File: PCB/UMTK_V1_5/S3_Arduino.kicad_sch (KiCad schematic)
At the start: 0 parts

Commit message: Put in Files for V1
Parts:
- added C10, C5, C6, C7, C8, C9: 0.1u, Ceramic Cap 5mm, symbol UMTK-altium-import:root_0_Cap
- added J1: NakedMega, Arduino Mega, symbol UMTK-altium-import:root_3_NakedMega
- added R33, R34, R35, R36, R37, R38, R39, R40, R41, R42, R43, R46, R48, R49, R50, R51: Res1, AXIAL-0.3-3D, symbol UMTK-altium-import:root_3_Res1
- added R44, R45, R47, R52, R53, R54, R55: Res1, AXIAL-0.3-3D, symbol UMTK-altium-import:root_0_Res1
- added SW1, SW2, SW3, SW4, SW5, SW6: Tac Switch, TacSwitch, symbol UMTK-altium-import:root_0_Tac Switch
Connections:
- new net: C8.1, R49.2, R53.1, SW4.2
- new net: R39.2, R40.1
- new net: R40.2, R41.1
- new net: C10.1, R51.2, R55.1, SW6.2
- new net: R33.2, R34.1
- new net: R34.2, R35.1
- new net: C9.1, R50.2, R54.1, SW5.2
- new net: C5.1, R43.2, R44.1, SW1.2
- new net: J1.D4, R37.1
- new net: C7.1, R48.2, R52.1, SW3.2
- new net: C6.1, R46.2, R47.1, SW2.2
- new net: J1.D3, R45.2
- new net +5: J1.EXT5V, R43.1, R46.1, R48.1, R49.1, R50.1, R51.1
- new net D1_A: J1.D33
- new net D1_B: J1.D35
- new net D1_C: J1.D29
- new net D1_D: J1.D31
- new net D1_D1: J1.D24
- new net D1_D2: J1.D25
- new net D1_D3: J1.D26
- new net D1_D4: J1.D27
- new net D1_DP: J1.D30
- new net D1_E: J1.D32
- new net D1_F: J1.D34
- new net D1_G: J1.D28
- new net D1_OE: J1.D36
- new net D2_A: J1.D42
- new net D2_B: J1.D44
- new net D2_C: J1.D38
- new net D2_D: J1.D40
- new net D2_DP: J1.D39
- new net D2_E: J1.D41
- new net D2_F: J1.D43
- new net D2_G: J1.D37
- new net D2_OE: J1.D45
- new net GND: C10.2, C5.2, C6.2, C7.2, C8.2, C9.2, J1.GND, R36.2, R38.2, R42.2, SW1.3, SW2.3, SW3.3, SW4.3, SW5.3, SW6.3
- new net LC_DT: J1.D6
- new net LC_SCK: J1.D5
- new net M_DISABLE: J1.D7
- new net M_EN/IN1: J1.D8
- new net M_FAULT: J1.D12
- new net M_ISENS: J1.A2
- new net M_ITRIP: J1.D10
- new net M_OL: J1.D11
- new net M_PH/IN2: J1.D9
- new net SLIDE_CLK: R37.2, R38.1
- new net SLIDE_DAT: R45.1
- new net SW_1: J1.A5, R52.2
- new net SW_2: J1.A6, R53.2
- new net SW_3: J1.A7, R54.2
- new net SW_4: J1.A8, R55.2
- new net SW_5: J1.A9, R44.2
- new net SW_6: J1.A10, R47.2
- new net Vin: R33.1
- new net Vin_sens: J1.A0, R35.2, R36.1
- new net Vmot: R39.1
- new net Vmot_sens: J1.A1, R41.2, R42.1
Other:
- note added: "Arduino"
- note added: "Buttons 1-4"
- note added: "Buttons 5-6"

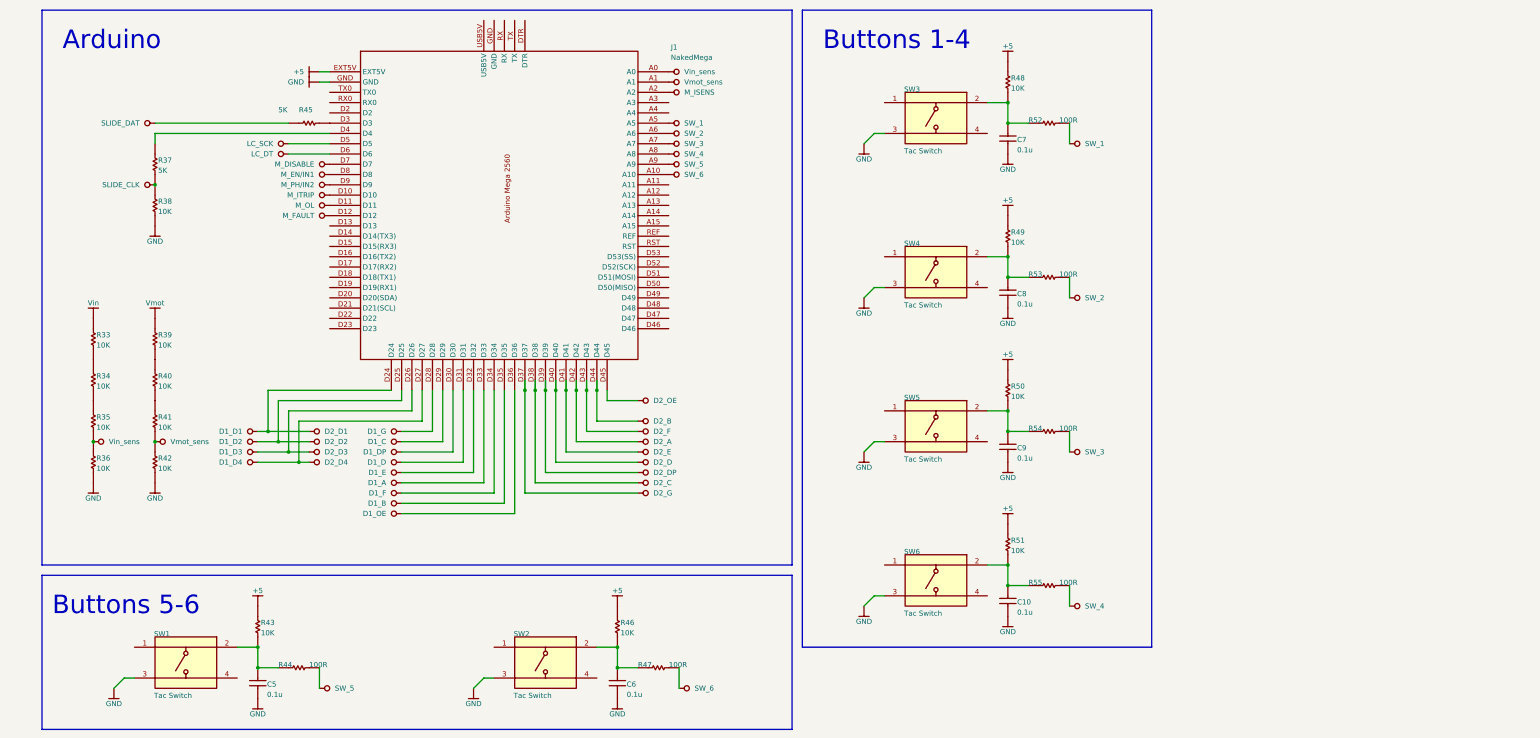
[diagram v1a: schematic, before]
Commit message: Updated Schematics
Done: 7 Seg, Power, Motor, Slide, HX711
To Do: Arduino
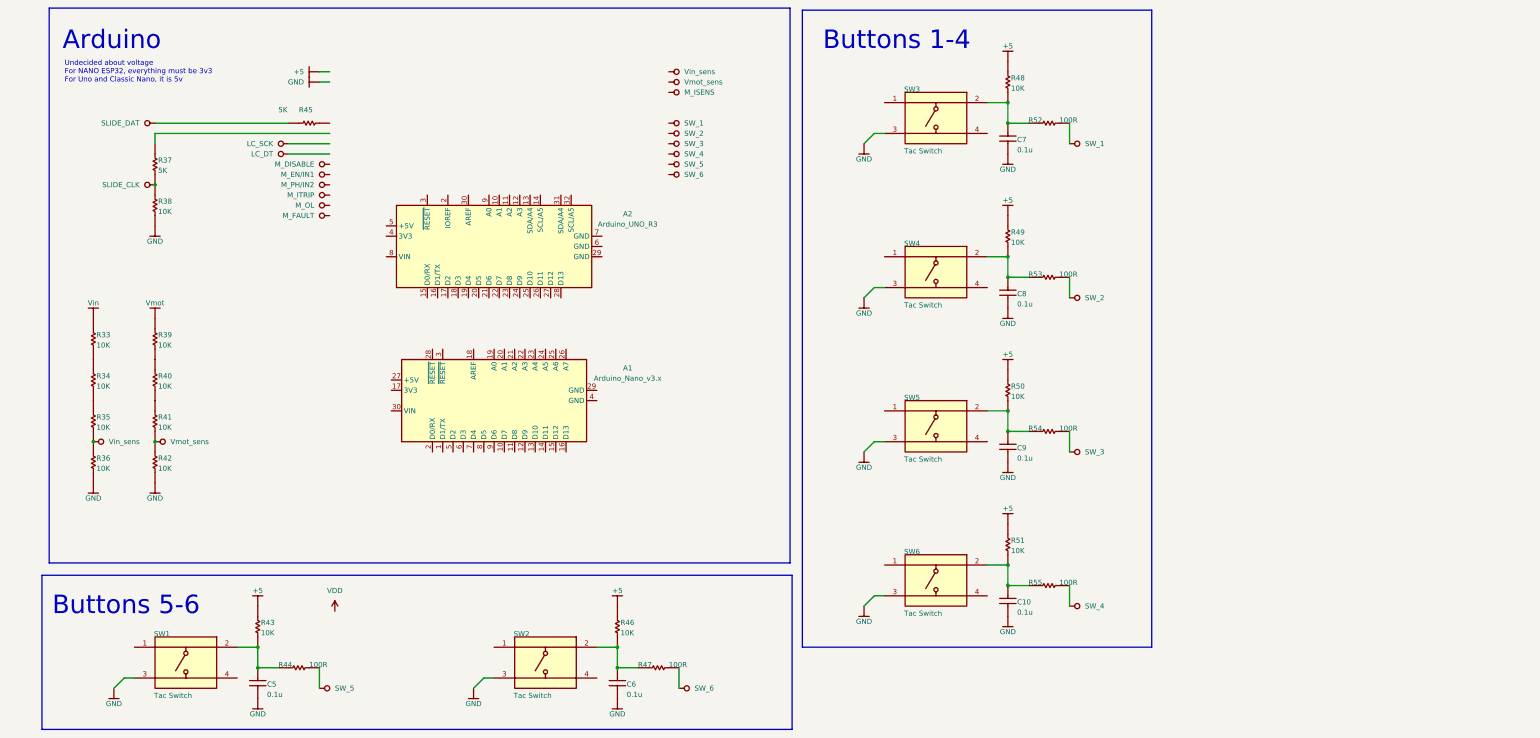
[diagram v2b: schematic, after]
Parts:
- removed J1: NakedMega, Arduino Mega, symbol UMTK-altium-import:root_3_NakedMega
- added A1: Arduino_Nano_v3.x, Module:Arduino_Nano, symbol MCU_Module:Arduino_Nano_v3.x
- added A2: Arduino_UNO_R3, Module:Arduino_UNO_R3, symbol MCU_Module:Arduino_UNO_R3
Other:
- note added: "Undecided about voltage For NANO ESP32, everything must be 3v3 For Uno and Classic Nano, it is 5v"

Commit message: Updating Schematic
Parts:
- removed A1: Arduino_Nano_v3.x, Module:Arduino_Nano, symbol MCU_Module:Arduino_Nano_v3.x
- removed A2: Arduino_UNO_R3, Module:Arduino_UNO_R3, symbol MCU_Module:Arduino_UNO_R3
- removed C10, C5, C6, C7, C8, C9: 0.1u, Ceramic Cap 5mm, symbol UMTK-altium-import:root_0_Cap
- removed R33, R34, R35, R36, R39, R40, R41, R42, R43, R46, R48, R49, R50, R51: Res1, AXIAL-0.3-3D, symbol UMTK-altium-import:root_3_Res1
- removed R44, R47, R52, R53, R54, R55: Res1, AXIAL-0.3-3D, symbol UMTK-altium-import:root_0_Res1
- removed SW1, SW2, SW3, SW4, SW5, SW6: Tac Switch, TacSwitch, symbol UMTK-altium-import:root_0_Tac Switch
- added A1: Arduino_Mega2560_R3_Shield, PCM_arduino-library:Arduino_Mega2560_R3_Shield, symbol arduino-library:Arduino_Mega2560_R3_Shield
- added C1, C2, C3, C4, C5, C6: 0.1u, symbol Device:C
- added R10, R12, R14, R15, R16, R17, R18, R19, R2, R20, R21, R4, R6, R8: 10k, symbol Device:R_US
- added R11, R13, R3, R5, R7, R9: 100r, symbol Device:R_US
- added S1, S2, S3, S4, S5, S6: FSM4JSMATR, digikey-footprints:Switch_Tactile_SMD_6x6mm, symbol dk_Tactile-Switches:FSM4JSMATR
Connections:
- net GND: now also C1.1, C2.1, C3.1, C4.1, C5.1, C6.1, R17.2, R21.2, S1.2, S2.2, S3.2, S4.2, S5.2, S6.2
- net SW_1: now also R5.2
- net SW_2: now also R7.2
- net SW_3: now also R9.2
- net SW_4: now also R11.2
- net SW_6: now also R13.2, R3.2
- net VDD: now also R10.2, R12.2, R2.2, R4.2, R6.2, R8.2
- new net: C1.2, R2.1, R3.1, S1.3
- new net: C4.2, R8.1, R9.1, S4.3
- new net: C5.2, R10.1, R11.1, S5.3
- new net: C6.2, R12.1, R13.1, S6.3
- new net: C3.2, R6.1, R7.1, S3.3
- new net: C2.2, R4.1, R5.1, S2.3
- new net: R14.2, R15.1
- new net: R15.2, R16.1
- new net: R18.2, R19.1
- new net: R19.2, R20.1
- new net +12V: R14.1
- new net VMOTOR: R18.1
- new net VM_Sense: R20.2, R21.1
- new net Vin_Sense: R16.2, R17.1
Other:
- note added: "Buttons"
- note removed: "Buttons 1-4"
- note removed: "Buttons 5-6"
- moved on the sheet: R37, R38, R45

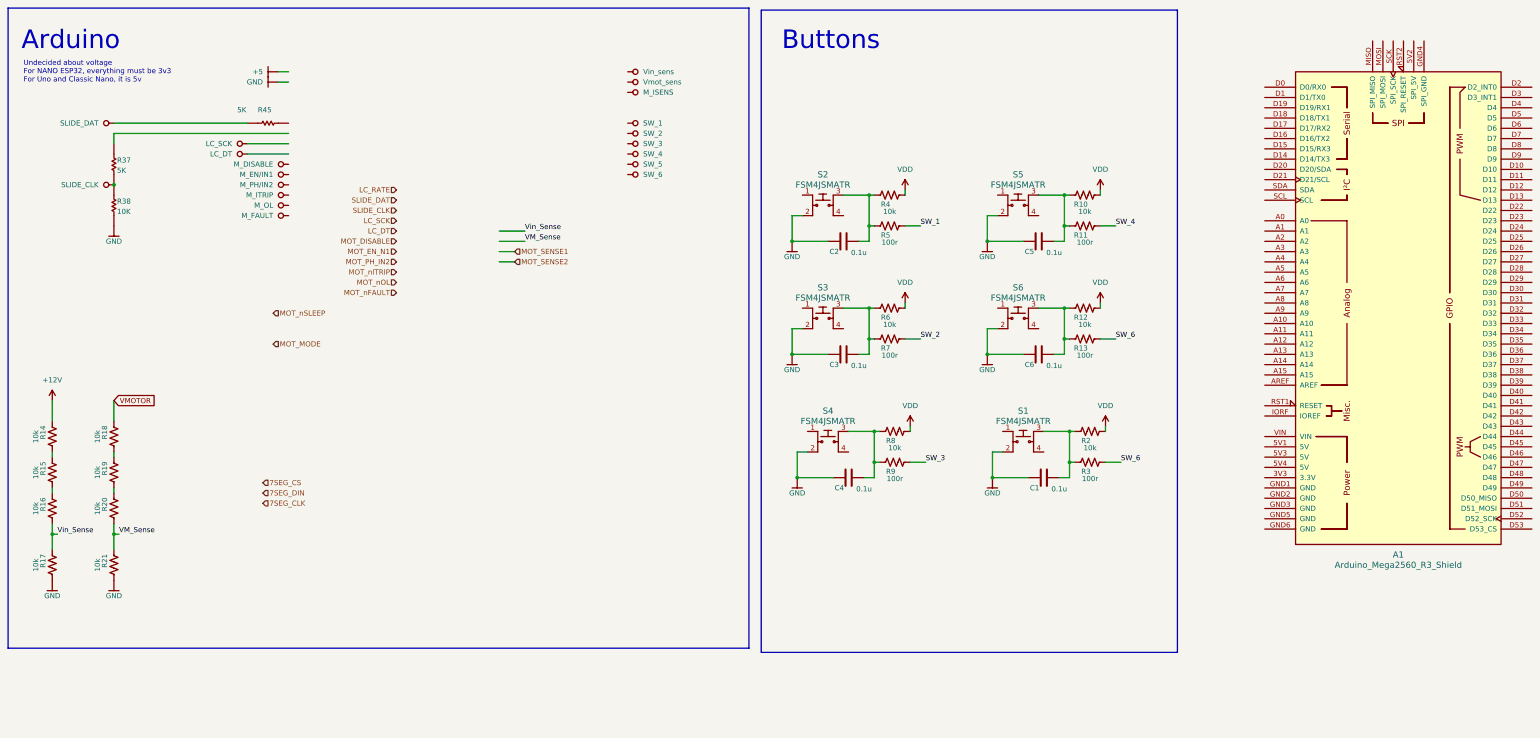
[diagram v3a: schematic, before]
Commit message: Schematic Done, Assigning footprint
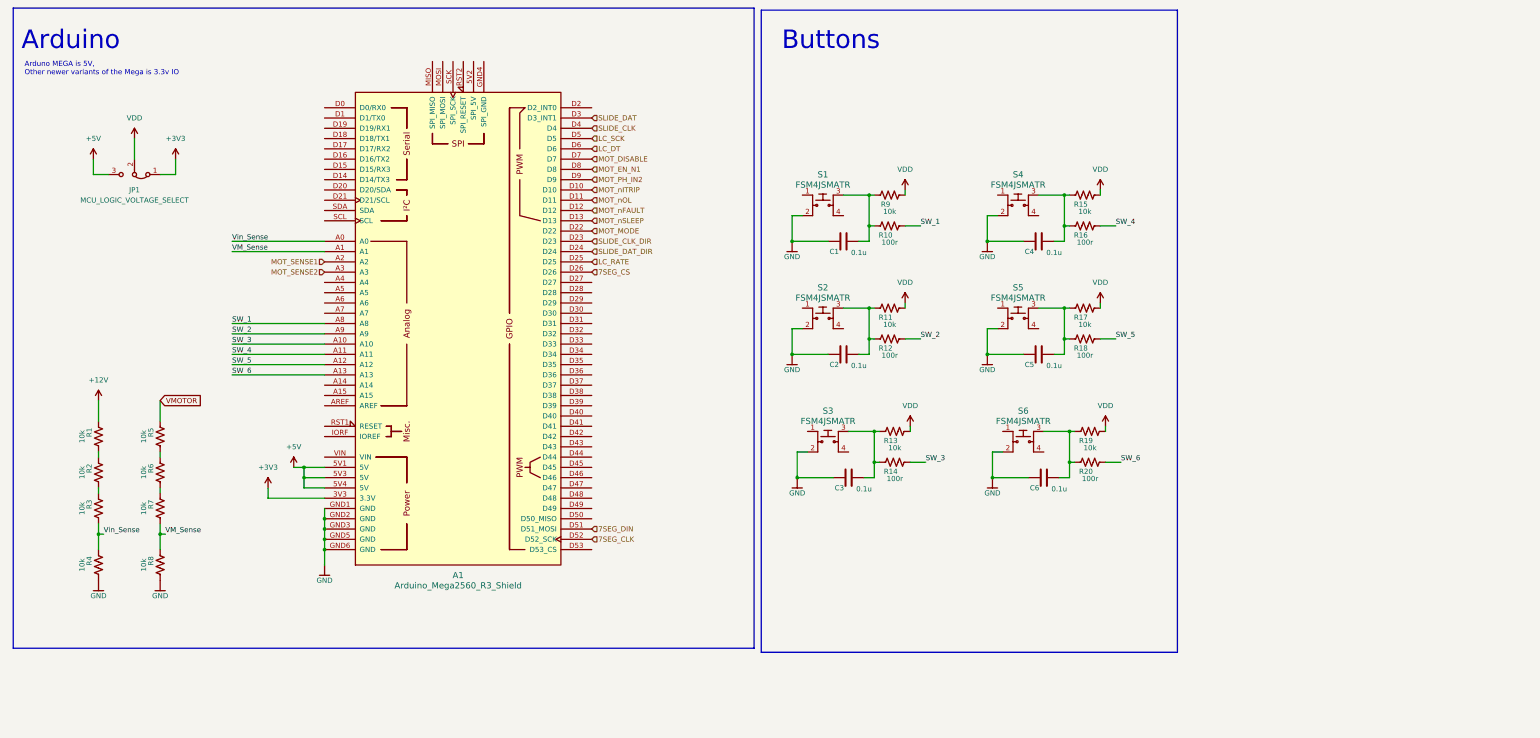
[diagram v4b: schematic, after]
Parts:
- removed R37, R38: Res1, AXIAL-0.3-3D, symbol UMTK-altium-import:root_3_Res1
- removed R45: Res1, AXIAL-0.3-3D, symbol UMTK-altium-import:root_0_Res1
- added JP1: MCU_LOGIC_VOLTAGE_SELECT, symbol Jumper:Jumper_3_Bridged12
- renumbered C2 to C1, C3 to C2, C4 to C3, C5 to C4, C6 to C5, C1 to C6, R14 to R1, R5 to R10, R6 to R11, R7 to R12, R8 to R13, R9 to R14, R10 to R15, R11 to R16, R12 to R17, R13 to R18, R2 to R19, R15 to R2, R3 to R20, R16 to R3, R17 to R4, R18 to R5, R19 to R6, R20 to R7, R21 to R8, R4 to R9, S2 to S1, S3 to S2, S4 to S3, S5 to S4, S6 to S5, S1 to S6
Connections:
- net 7SEG_CLK: now also A1.D52 (D52_SCK)
- net 7SEG_CS: now also A1.D26
- net 7SEG_DIN: now also A1.D51 (D51_MOSI)
- net GND: now also A1.GND1 (GND), A1.GND2 (GND), A1.GND3 (GND), A1.GND5 (GND), A1.GND6 (GND)
- net LC_DT: now also A1.D6
- net LC_RATE: now also A1.D25
- net LC_SCK: now also A1.D5
- net MOT_DISABLE: now also A1.D7
- net MOT_EN_N1: now also A1.D8
- net MOT_MODE: now also A1.D22
- net MOT_PH_IN2: now also A1.D9
- net MOT_SENSE1: now also A1.A2
- net MOT_SENSE2: now also A1.A3
- net MOT_nFAULT: now also A1.D12
- net MOT_nITRIP: now also A1.D10
- net MOT_nOL: now also A1.D11
- net MOT_nSLEEP: now also A1.D13
- net SLIDE_CLK: now also A1.D4
- net SLIDE_DAT: now also A1.D3 (D3_INT1)
- net SW_1: now also A1.A8
- net SW_2: now also A1.A9
- net SW_3: now also A1.A10
- net SW_4: now also A1.A11
- net SW_5: now also A1.A12, R18.2
- net SW_6: now also A1.A13; no longer R18.2
- net VDD: now also JP1.2 (C)
- net VM_Sense: now also A1.A1
- net Vin_Sense: now also A1.A0
- net +3V3: now reaches A1.3V3 (3.3V)
- net +3V3: now also JP1.1 (A)
- net +5V: now reaches A1.5V1 (5V)
- net +5V: now also A1.5V3 (5V), A1.5V4 (5V), JP1.3 (B)
- net SLIDE_CLK_DIR: now reaches A1.D23
- net SLIDE_DAT_DIR: now reaches A1.D24
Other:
- note added: "Arduno MEGA is 5V, Other newer variants of the Mega is 3.3v IO"
- note removed: "Undecided about voltage For NANO ESP32, everything must be 3v3 For Uno and Classic Nano, it is 5v"
- moved on the sheet: A1, R1, R2, R3, R4, R5, R6, R7, R8

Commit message: Footprint assign
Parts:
- A1: footprint PCM_arduino-library:Arduino_Mega2560_R3_Shield -> arduino-library:Arduino_Mega2560_R3_Shield
- C1, C2, C3, C4, C5, C6: footprint (none) -> Capacitor_SMD:C_0402_1005Metric
- JP1: footprint (none) -> Jumper:SolderJumper-3_P1.3mm_Bridged12_Pad1.0x1.5mm
- R1, R10, R11, R12, R13, R14, R15, R16, R17, R18, R19, R2, R20, R3, R4, R5, R6, R7, R8, R9: footprint (none) -> Resistor_SMD:R_0402_1005Metric
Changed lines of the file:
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@@
 			)
 		)
-		(property "Footprint" ""
+		(property "Footprint" "Resistor_SMD:R_0402_1005Metric"
 			(at 222.504 131.064 90)
 			(effects
@@
 			)
 		)
-		(property "Footprint" ""
+		(property "Footprint" "Capacitor_SMD:C_0402_1005Metric"
 			(at 261.62 76.5048 0)
 			(effects
@@
 			)
 		)
-		(property "Footprint" ""
+		(property "Footprint" "Resistor_SMD:R_0402_1005Metric"
 			(at 269.494 65.024 90)
 			(effects
@@
 			)
 		)
-		(property "Footprint" ""
+		(property "Footprint" "Resistor_SMD:R_0402_1005Metric"
 			(at 26.416 157.734 90)
 			(effects
@@
 			)
 		)
-		(property "Footprint" ""
+		(property "Footprint" "Resistor_SMD:R_0402_1005Metric"
 			(at 269.494 92.964 90)
 			(effects
@@
 			)
 		)
-		(property "Footprint" ""
+		(property "Footprint" "Capacitor_SMD:C_0402_1005Metric"
 			(at 261.62 104.4448 0)
 			(effects
@@
 			)
 		)
-		(property "Footprint" ""
+		(property "Footprint" "Capacitor_SMD:C_0402_1005Metric"
 			(at 213.36 76.5048 0)
 			(effects
@@
 			)
 		)
-		(property "Footprint" ""
+		(property "Footprint" "Resistor_SMD:R_0402_1005Metric"
 			(at 270.764 131.064 90)
 			(effects
@@
 			)
 		)
-		(property "Footprint" ""
+		(property "Footprint" "Resistor_SMD:R_0402_1005Metric"
 			(at 26.416 134.874 90)
 			(effects
@@
 			)
 		)
-		(property "Footprint" ""
+		(property "Footprint" "Jumper:SolderJumper-3_P1.3mm_Bridged12_Pad1.0x1.5mm"
 			(at 34.29 60.96 0)
 			(effects
@@
 			)
 		)
-		(property "Footprint" ""
+		(property "Footprint" "Resistor_SMD:R_0402_1005Metric"
 			(at 221.234 92.964 90)
 			(effects
@@
 			)
 		)
-		(property "Footprint" ""
+		(property "Footprint" "Resistor_SMD:R_0402_1005Metric"
 			(at 270.764 123.444 90)
 			(effects
@@
 			)
 		)
-		(property "Footprint" ""
+		(property "Footprint" "Resistor_SMD:R_0402_1005Metric"
 			(at 41.656 157.734 90)
 			(effects
@@
 			)
 		)
-		(property "Footprint" ""
+		(property "Footprint" "Resistor_SMD:R_0402_1005Metric"
 			(at 269.494 100.584 90)
 			(effects
@@
 			)
 		)
-		(property "Footprint" ""
+		(property "Footprint" "Resistor_SMD:R_0402_1005Metric"
 			(at 41.656 125.984 90)
 			(effects
@@
 			)
 		)
-		(property "Footprint" ""
+		(property "Footprint" "Resistor_SMD:R_0402_1005Metric"
 			(at 221.234 100.584 90)
 			(effects
@@
 			)
 		)
-		(property "Footprint" ""
+		(property "Footprint" "Capacitor_SMD:C_0402_1005Metric"
 			(at 213.36 104.4448 0)
 			(effects
@@
 			)
 		)
-		(property "Footprint" ""
+		(property "Footprint" "Capacitor_SMD:C_0402_1005Metric"
 			(at 262.89 134.9248 0)
 			(effects
@@
 			)
 		)
-		(property "Footprint" ""
+		(property "Footprint" "Resistor_SMD:R_0402_1005Metric"
 			(at 269.494 72.644 90)
 			(effects
@@
 			)
 		)
-		(property "Footprint" ""
+		(property "Footprint" "Resistor_SMD:R_0402_1005Metric"
 			(at 41.656 143.764 90)
 			(effects
@@
 			)
 		)
-		(property "Footprint" ""
+		(property "Footprint" "Resistor_SMD:R_0402_1005Metric"
 			(at 41.656 134.874 90)
 			(effects
@@
 			)
 		)
-		(property "Footprint" ""
+		(property "Footprint" "Capacitor_SMD:C_0402_1005Metric"
 			(at 214.63 134.9248 0)
 			(effects
@@
 			)
 		)
-		(property "Footprint" ""
+		(property "Footprint" "Resistor_SMD:R_0402_1005Metric"
 			(at 222.504 123.444 90)
 			(effects
@@
 			)
 		)
-		(property "Footprint" ""
+		(property "Footprint" "Resistor_SMD:R_0402_1005Metric"
 			(at 26.416 143.764 90)
 			(effects
@@
 			)
 		)
-		(property "Footprint" ""
+		(property "Footprint" "Resistor_SMD:R_0402_1005Metric"
 			(at 221.234 65.024 90)
 			(effects
@@
 			)
 		)
-		(property "Footprint" ""
+		(property "Footprint" "Resistor_SMD:R_0402_1005Metric"
 			(at 221.234 72.644 90)
 			(effects
@@
 			)
 		)
-		(property "Footprint" "PCM_arduino-library:Arduino_Mega2560_R3_Shield"
+		(property "Footprint" "arduino-library:Arduino_Mega2560_R3_Shield"
 			(at 114.3 172.72 0)
 			(effects
@@
 			)
 		)
-		(property "Footprint" ""
+		(property "Footprint" "Resistor_SMD:R_0402_1005Metric"
 			(at 26.416 125.984 90)
 			(effects

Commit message: ERC good, imported into PCB
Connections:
- no-connect marks 0 -> 66
